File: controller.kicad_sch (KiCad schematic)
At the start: 46 parts, among them J1 Conn_ST_STDC14, J2 USB_C_Receptacle_USB2.0_14P, SW1 SW_Push, SW10 SW_Push, SW11 SW_Push, SW2 SW_Push, SW3 SW_Push, SW4 SW_Push, SW5 SW_Push, SW6 SW_Push, SW8 SW_Push, SW9 SW_Push, U1 STM32L476RGTx, U2 BD33FC0FP, U3 NUP2202

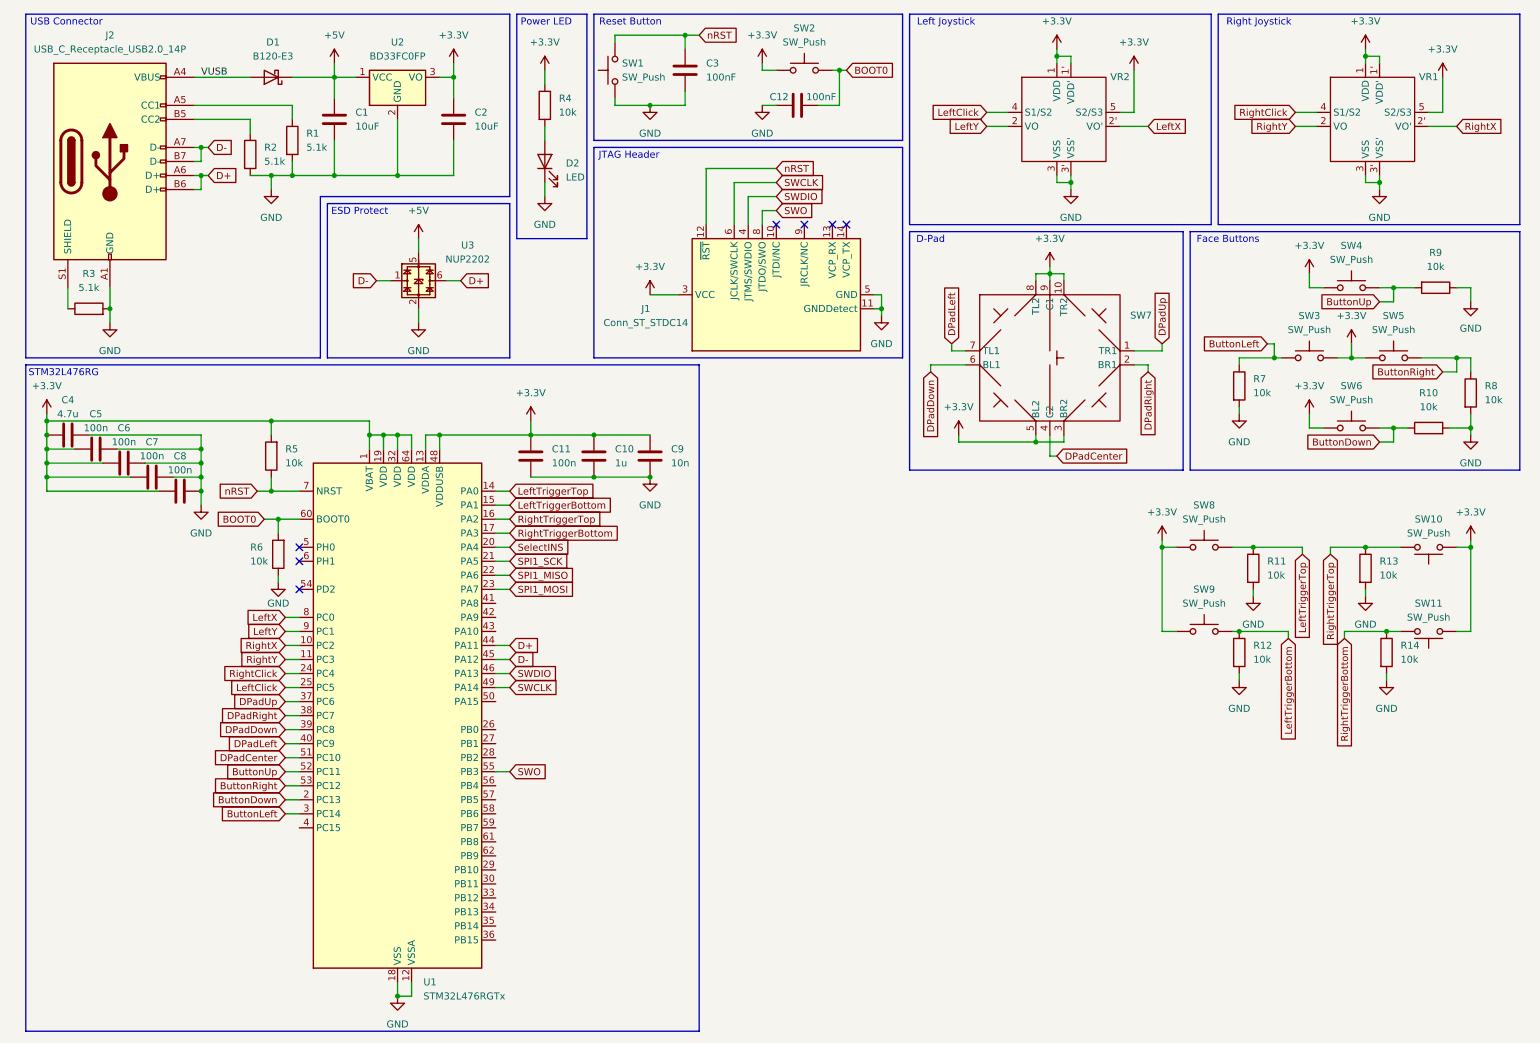
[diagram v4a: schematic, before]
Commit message: add start and select + resistors to all other buttons
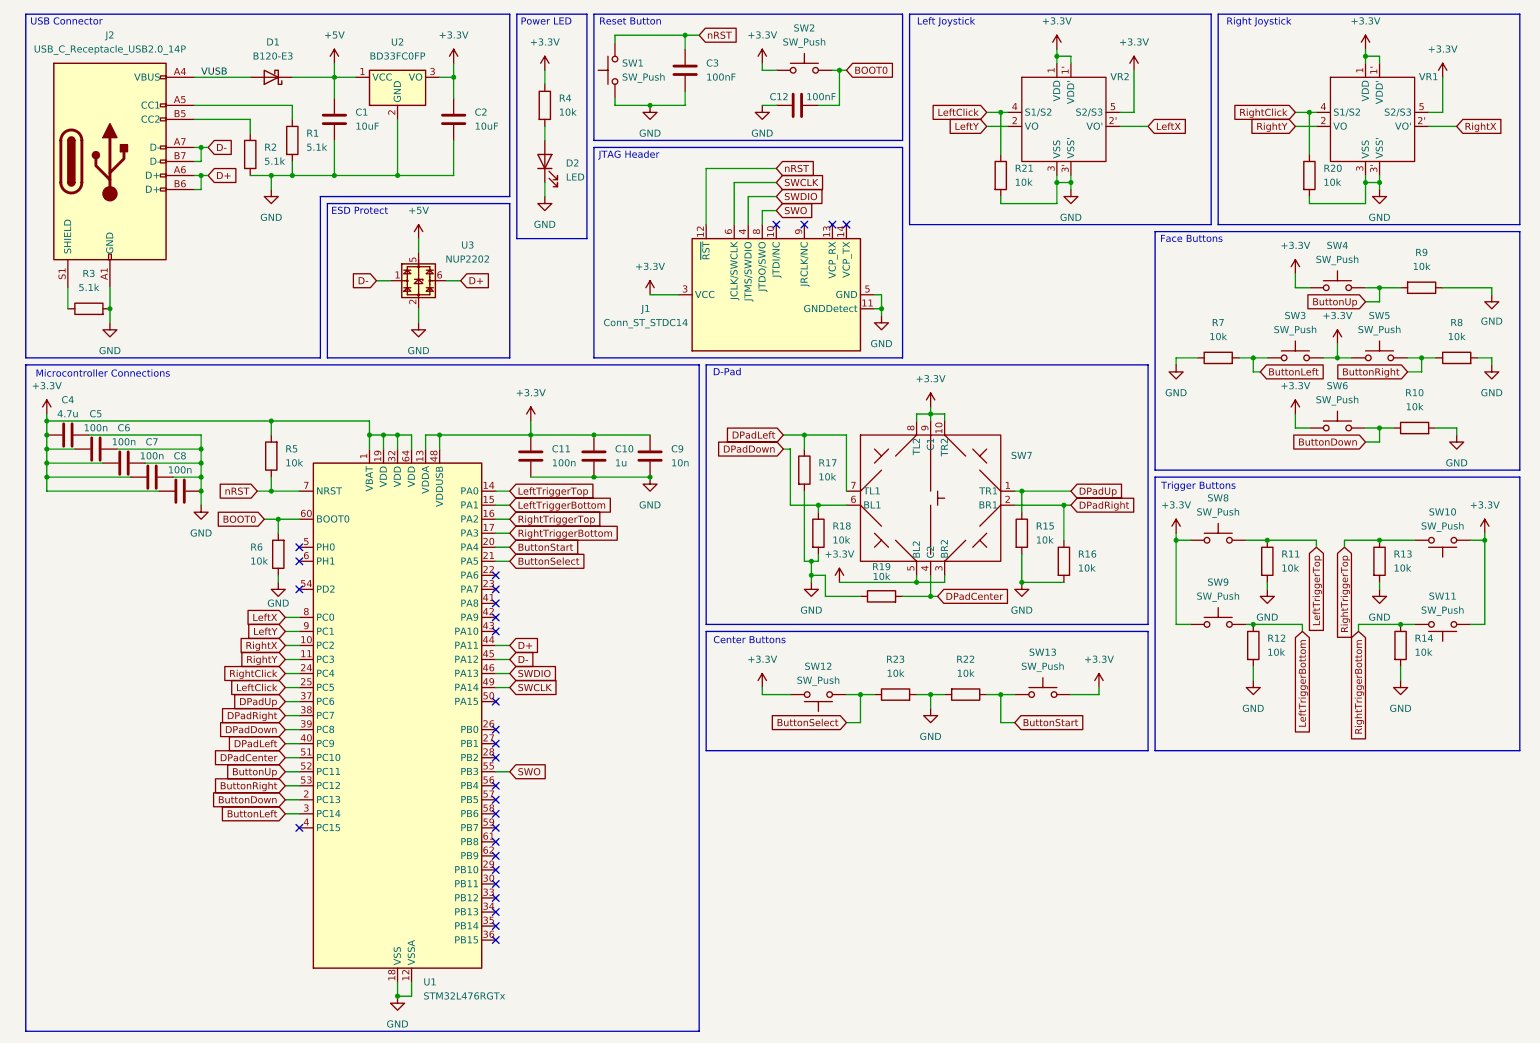
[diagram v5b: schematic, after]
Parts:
- added R15, R16, R17, R18, R19, R20, R21, R22, R23: 10k, Resistor_SMD:R_0201_0603Metric, symbol Device:R
- added SW12, SW13: SW_Push, Button_Switch_THT:SW_PUSH_6mm, symbol Switch:SW_Push
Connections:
- net +3.3V: now also SW12.2, SW13.2
- net ButtonLeft: now also R7.2; no longer R7.1
- net DPadCenter: now also R19.2
- net DPadDown: now also R18.1
- net DPadLeft: now also R17.1
- net DPadRight: now also R16.1
- net DPadUp: now also R15.1
- net GND: now also R7.1, R15.2, R16.2, R17.2, R18.2, R19.1, R20.2, R21.2, R22.2, R23.2; no longer R7.2
- net LeftClick: now also R21.1
- net RightClick: now also R20.1
- net SPI1_MISO: no longer names the net of U1.22 (PA6)
- net SPI1_MOSI: no longer names the net of U1.23 (PA7)
- net SPI1_SCK renamed ButtonSelect
- net ButtonSelect: now also R23.1, SW12.1
- net SelectINS renamed ButtonStart
- net ButtonStart: now also R22.1, SW13.1
- no-connect marks 7 -> 29
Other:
- note added: "Center Buttons"
- note added: "Microcontroller Connections"
- note added: "Trigger Buttons"
- note removed: "STM32L476RG"
- moved on the sheet: R10, R11, R12, R13, R14, R7, R8, R9, SW10, SW11, SW3, SW4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

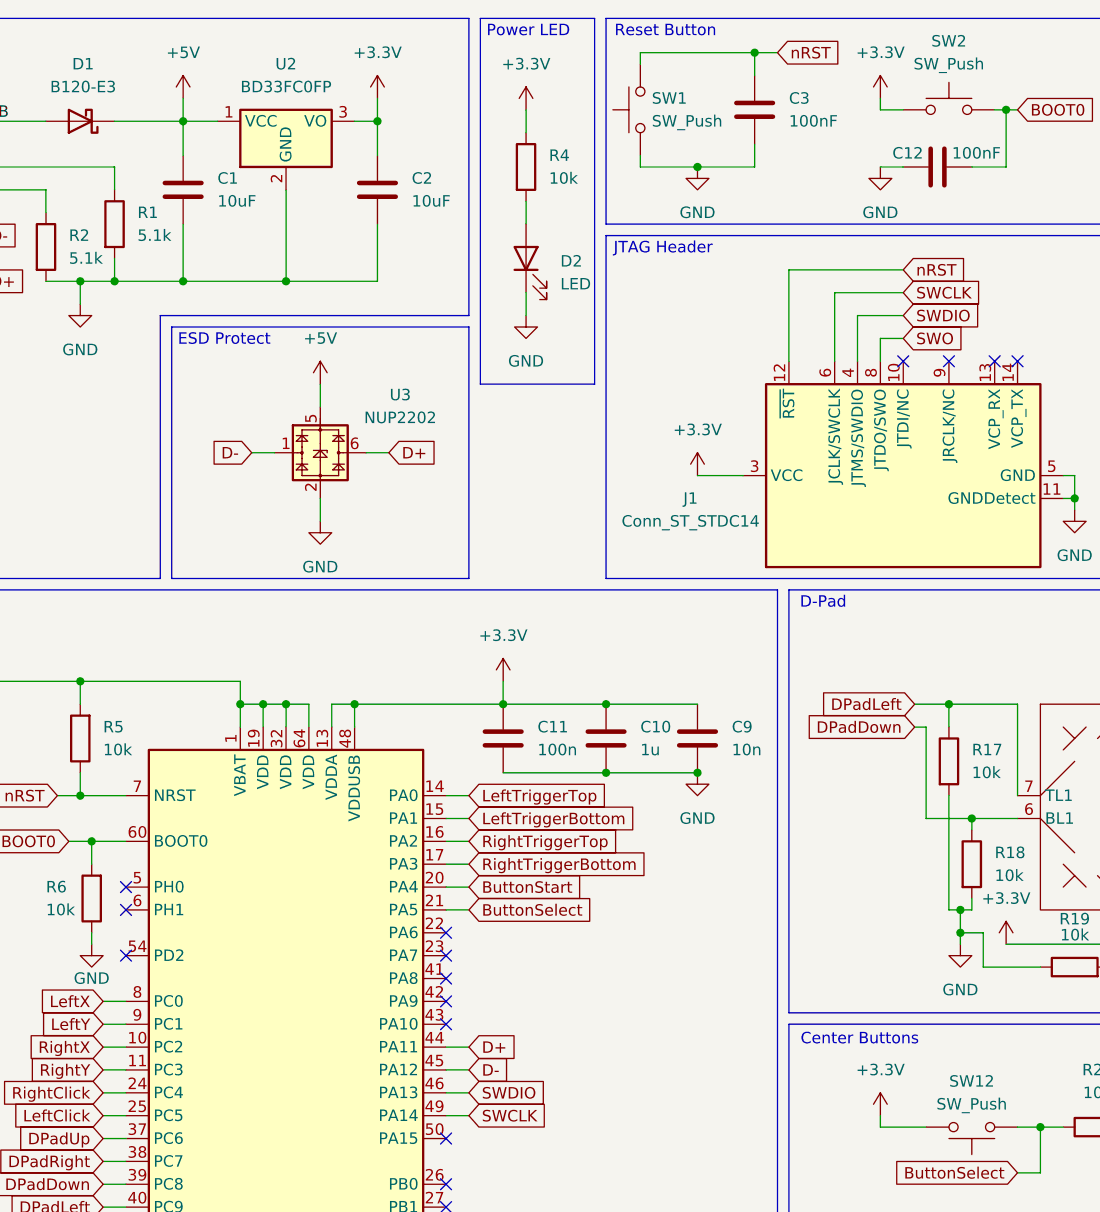
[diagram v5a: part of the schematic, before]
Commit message: fix ERC and add metadata
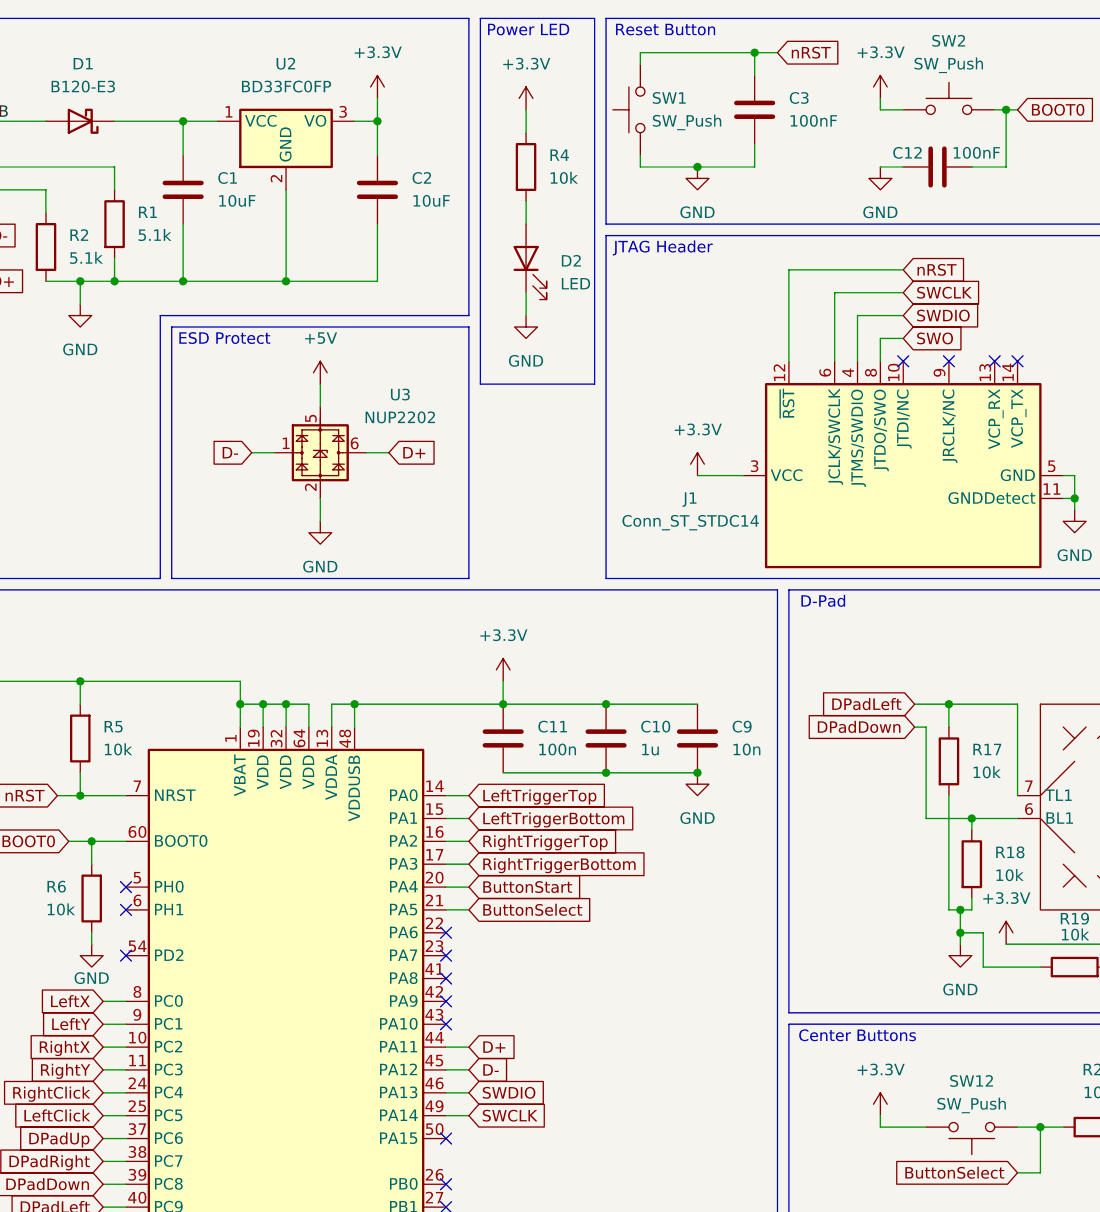
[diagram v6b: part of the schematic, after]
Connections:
- net +5V: no longer C1.1, D1.1 (K), U2.1 (VCC)
- new net: C1.1, D1.1 (K), U2.1 (VCC)
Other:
- company: (none) -> USU
- title: (none) -> USB Gamepad Controller
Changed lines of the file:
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@@
 	(generator_version "9.0")
 	(paper "A4")
+	(title_block
+		(title "USB Gamepad Controller")
+		(date "2025-11-02")
+		(rev "${REVISION}")
+		(company "USU")
+		(comment 1 "Richard Snider (CodeTriangle)")
+	)
 	(rectangle
 		(start 115.57 36.83)
@@
 	(text "Center Buttons"
 		(exclude_from_sim no)
-		(at 143.764 126.238 0)
+		(at 143.51 125.984 0)
 		(effects
 			(font
@@
 	)
 	(junction
+		(at 68.58 24.13)
+		(diameter 0)
+		(color 0 0 0 0)
+	)
+	(junction
 		(at 255.27 20.32)
 		(diameter 0)
@@
 	)
 	(junction
-		(at 68.58 24.13)
-		(diameter 0)
-		(color 0 0 0 0)
-	)
-	(junction
 		(at 58.42 104.14)
 		(diameter 0)
@@
 	(wire
 		(pts
-			(xy 167.64 63.5) (xy 167.64 66.04)
+			(xy 68.58 24.13) (xy 72.39 24.13)
 		)
 		(stroke
@@
 	(wire
 		(pts
-			(xy 265.43 74.93) (xy 265.43 77.47)
+			(xy 167.64 63.5) (xy 167.64 66.04)
 		)
 		(stroke
@@
 	(wire
 		(pts
-			(xy 97.79 104.14) (xy 100.33 104.14)
+			(xy 265.43 74.93) (xy 265.43 77.47)
 		)
 		(stroke
@@
 	(wire
 		(pts
-			(xy 58.42 104.14) (xy 58.42 106.68)
+			(xy 97.79 104.14) (xy 100.33 104.14)
 		)
 		(stroke
@@
 	(wire
 		(pts
-			(xy 160.02 115.57) (xy 173.99 115.57)
+			(xy 58.42 104.14) (xy 58.42 106.68)
 		)
 		(stroke
@@
 	(wire
 		(pts
-			(xy 68.58 24.13) (xy 72.39 24.13)
+			(xy 160.02 115.57) (xy 173.99 115.57)
 		)
 		(stroke
@@
 	(wire
 		(pts
-			(xy 68.58 24.13) (xy 68.58 21.59)
-		)
-		(stroke
-			(width 0)
-			(type default)
-		)
-	)
-	(wire
-		(pts
 			(xy 125.73 29.21) (xy 132.08 29.21)
 		)
@@
 					(unit 1)
 				)
-			)
-		)
-	)
-	(symbol
-		(lib_id "power:+5V")
-		(at 68.58 21.59 0)
-		(unit 1)
-		(exclude_from_sim no)
-		(in_bom yes)
-		(on_board yes)
-		(dnp no)
-		(fields_autoplaced yes)
-		(property "Reference" "#PWR06"
-			(at 68.58 25.4 0)
-			(effects
-				(font
-					(size 1.27 1.27)
-				)
-				(hide yes)
-			)
-		)
-		(property "Value" "+5V"
-			(at 68.58 16.51 0)
-			(effects
-				(font
-					(size 1.27 1.27)
-				)
-			)
-		)
-		(property "Footprint" ""
-			(at 68.58 21.59 0)
-			(effects
-				(font
-					(size 1.27 1.27)
-				)
-				(hide yes)
-			)
-		)
-		(property "Datasheet" ""
-			(at 68.58 21.59 0)
-			(effects
-				(font
-					(size 1.27 1.27)
-				)
-				(hide yes)
-			)
-		)
-		(property "Description" "Power symbol creates a global label with name \"+5V\""
-			(at 68.58 21.59 0)
-			(effects
-				(font
-					(size 1.27 1.27)
-				)
-				(hide yes)
-			)
-		)
-		(pin "1"
-		)
-		(instances
-			(project "controller"
-				(path "/8767df91-471e-42dd-a6da-5f13f49512a3"
-					(reference "#PWR06")
-					(unit 1)
-				)

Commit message: add fabrication files
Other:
- title: USB Gamepad Controller -> ${TITLE}
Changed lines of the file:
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@@
 	(paper "A4")
 	(title_block
-		(title "USB Gamepad Controller")
+		(title "${TITLE}")
 		(date "2025-11-02")
 		(rev "${REVISION}")
 		(company "USU")
-		(comment 1 "Richard Snider (CodeTriangle)")
+		(comment 1 "${AUTHOR}")
 	)
 	(rectangle

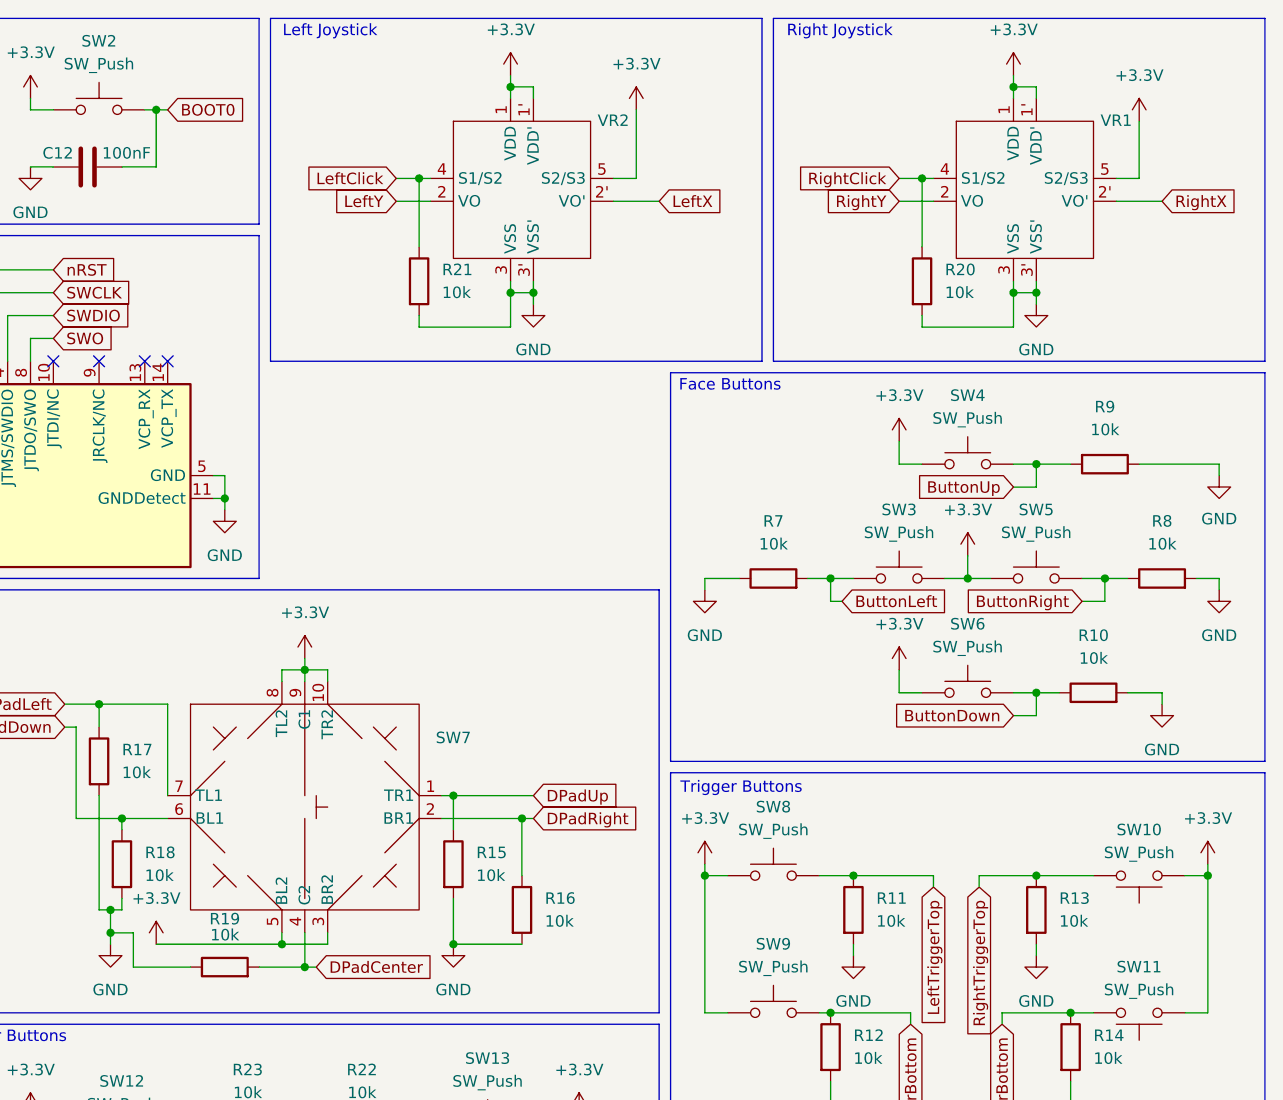
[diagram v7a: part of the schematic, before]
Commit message: set DNP flags
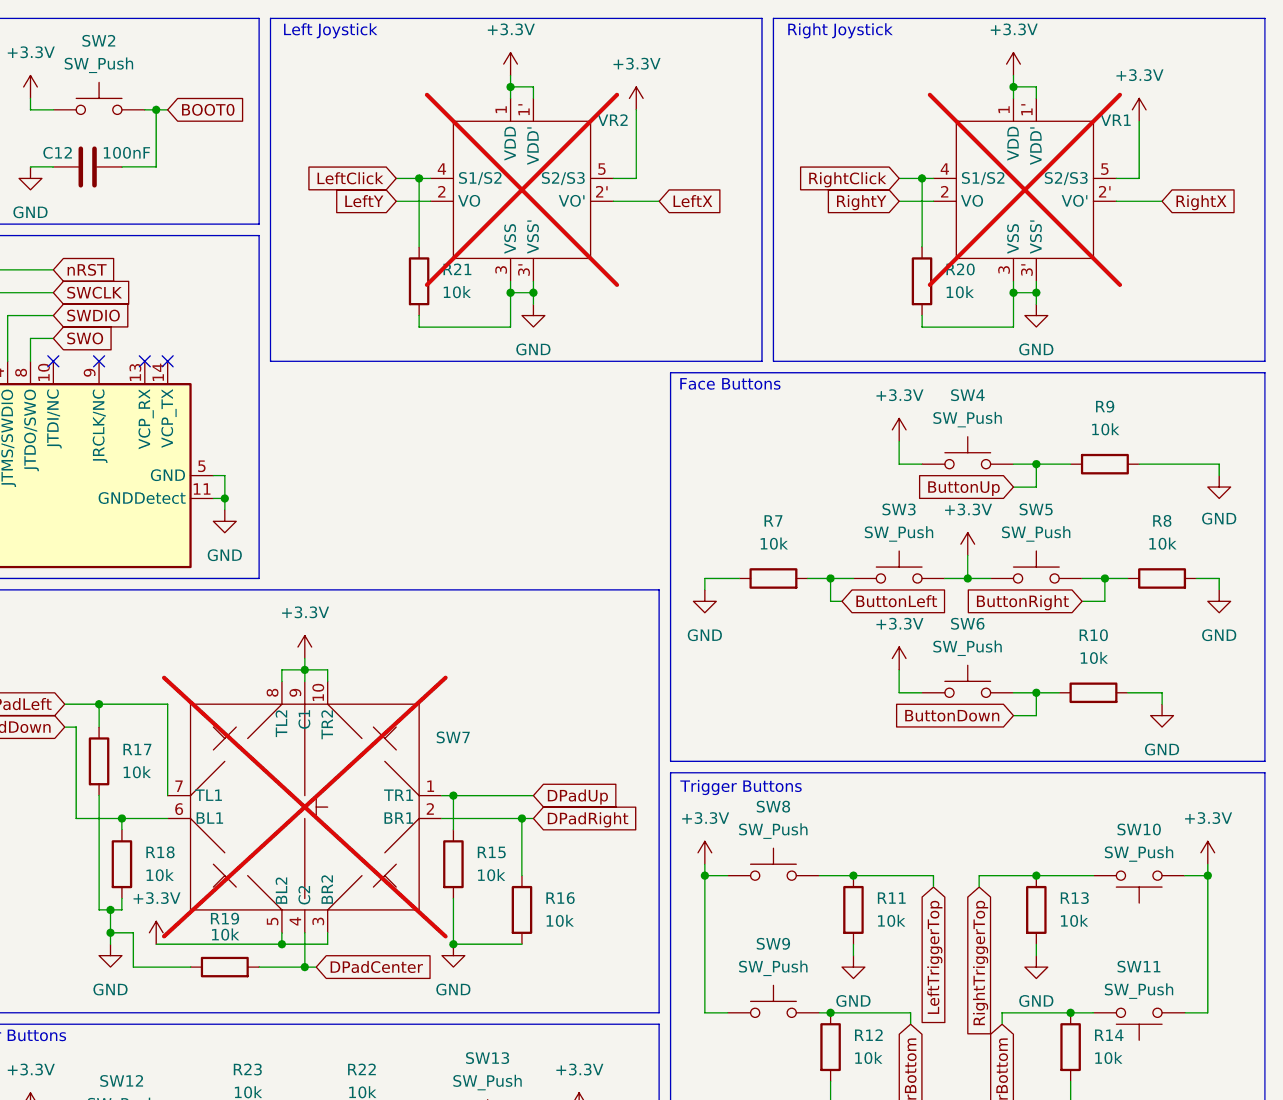
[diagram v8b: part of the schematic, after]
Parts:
- SW7, VR1, VR2: now not fitted
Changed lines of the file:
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@@
 		(in_bom yes)
 		(on_board yes)
-		(dnp no)
+		(dnp yes)
 		(fields_autoplaced yes)
 		(property "Reference" "VR1"
@@
 		(in_bom yes)
 		(on_board yes)
-		(dnp no)
+		(dnp yes)
 		(fields_autoplaced yes)
 		(property "Reference" "SW7"
@@
 		(in_bom yes)
 		(on_board yes)
-		(dnp no)
+		(dnp yes)
 		(fields_autoplaced yes)
 		(property "Reference" "VR2"
